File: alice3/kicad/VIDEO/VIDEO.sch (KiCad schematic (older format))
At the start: 14 parts, among them SW1 SW_PUSH, U1 Propeller_P8X32A-D40, U2 VGA_daughter_board, U3 24LC256, U4 Propeller_Plug, U5 LM2937-3.3, Y1 5 MHz

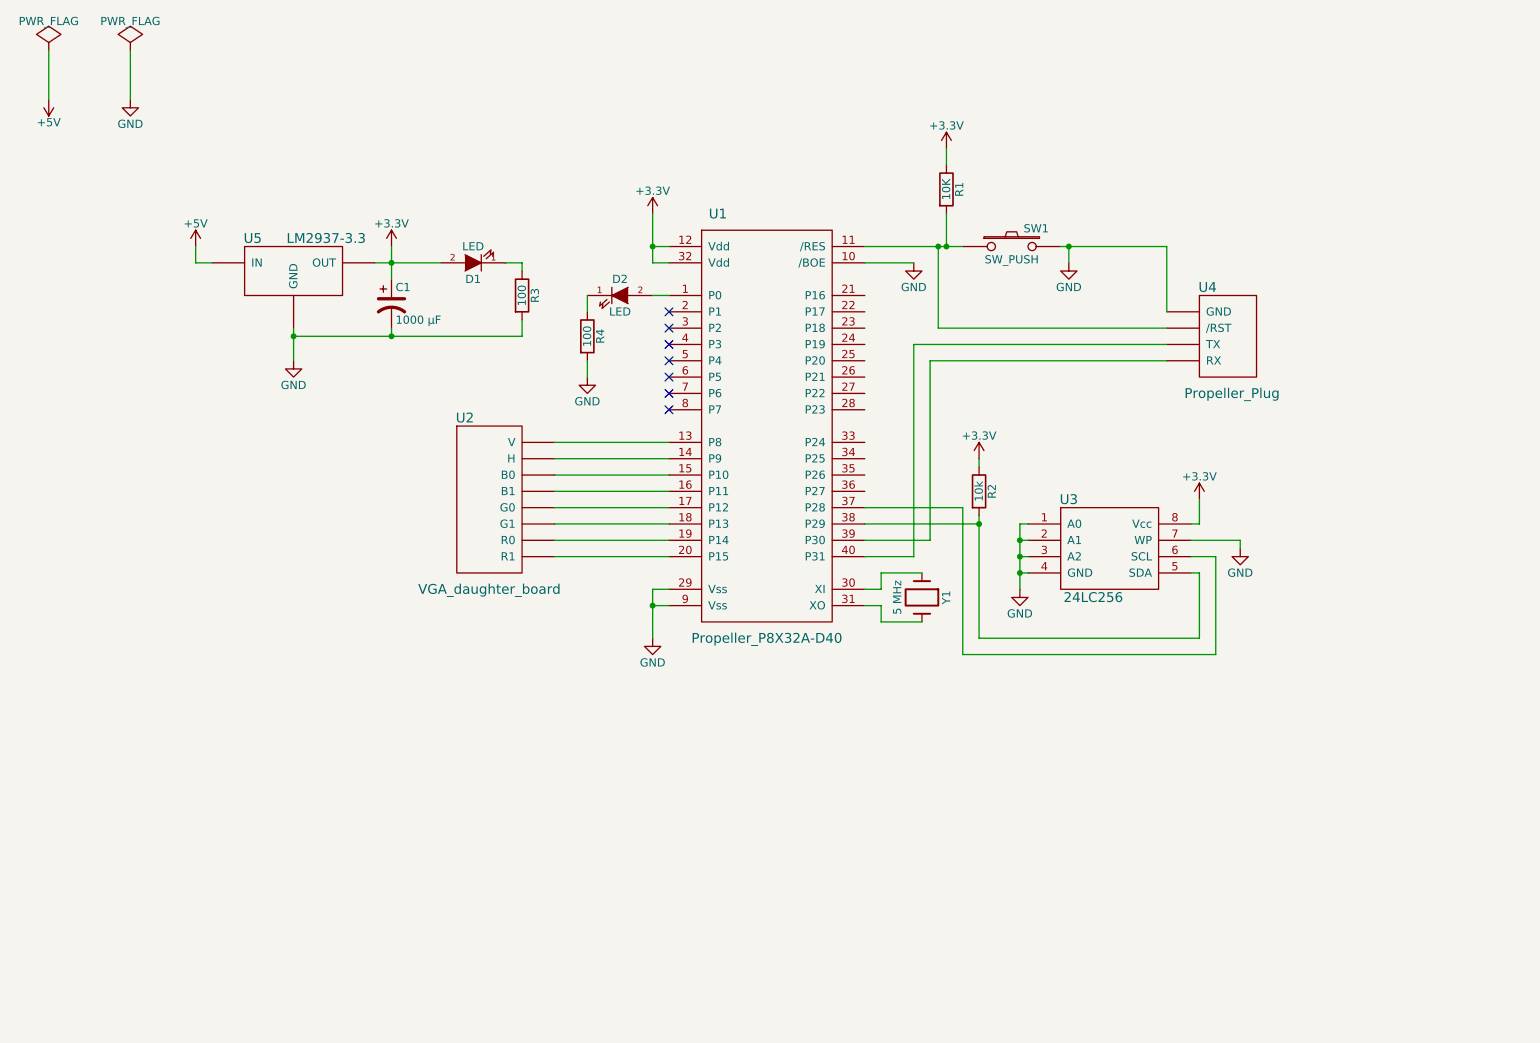
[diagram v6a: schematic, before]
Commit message: Add level shifters to video board.
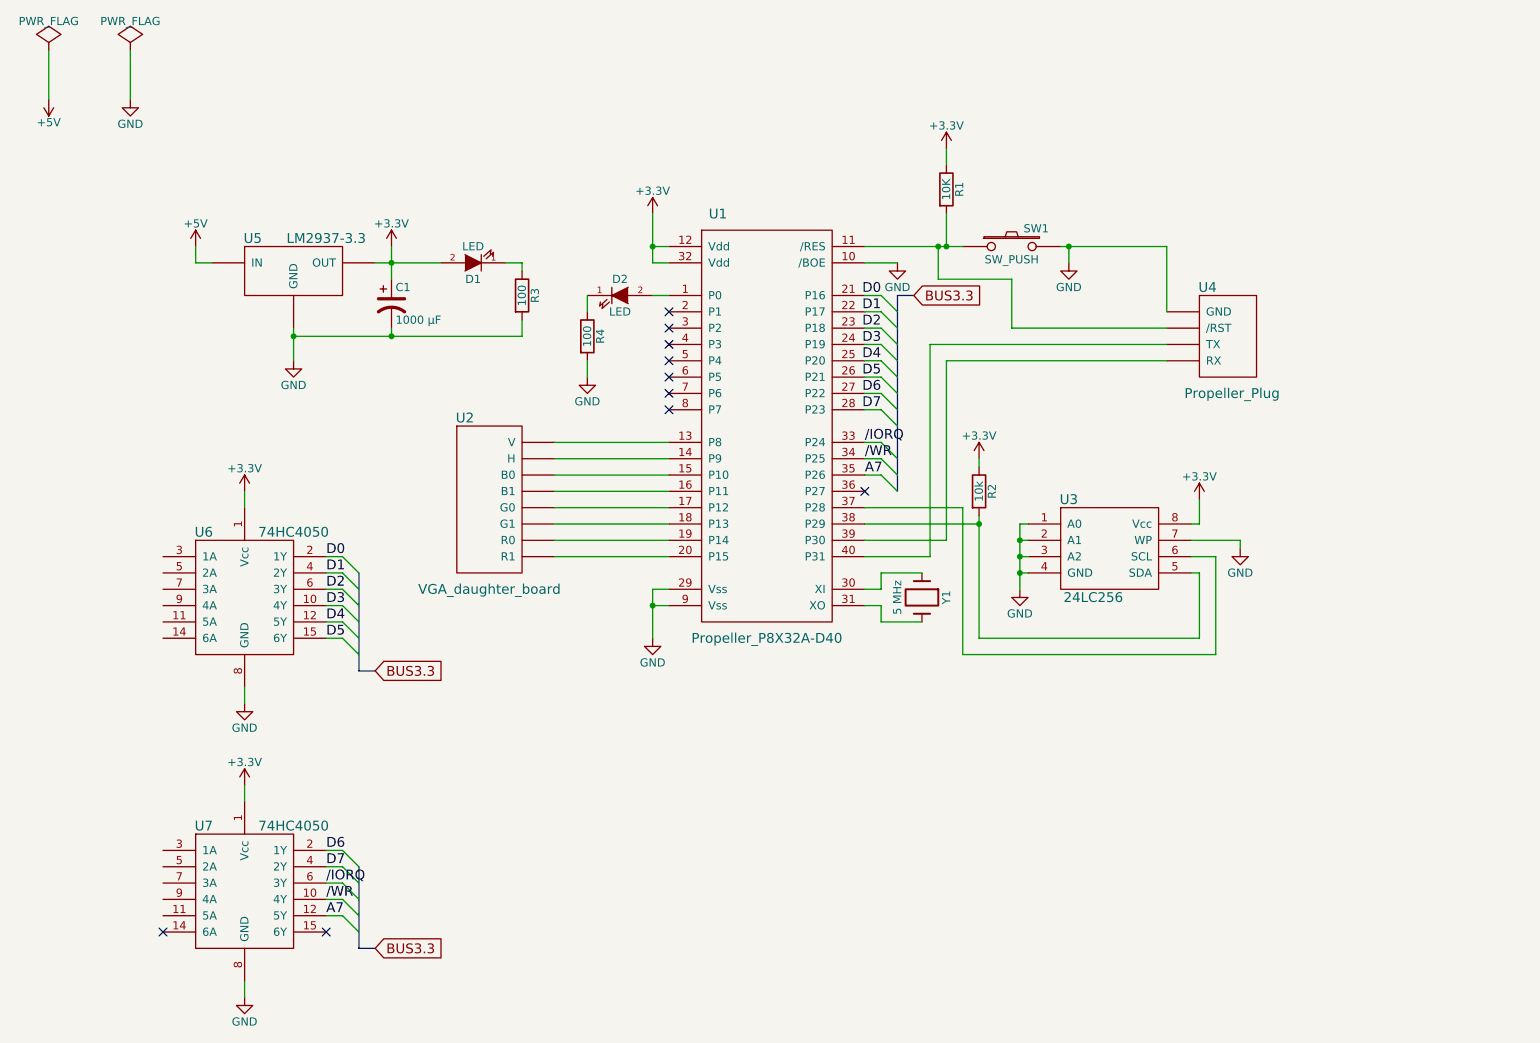
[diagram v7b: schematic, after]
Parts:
- added U6, U7: 74HC4050, symbol 74HC4050
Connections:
- net +3V3: now also U6.1 (Vcc), U7.1 (Vcc)
- net GND: now also U6.8 (GND), U7.8 (GND)
- net D0: now reaches U1.21 (P16)
- net D0: now also U6.2 (1Y)
- net D1: now reaches U1.22 (P17)
- net D1: now also U6.4 (2Y)
- net D2: now reaches U1.23 (P18)
- net D2: now also U6.6 (3Y)
- net D3: now reaches U1.24 (P19)
- net D3: now also U6.10 (4Y)
- net D4: now reaches U1.25 (P20)
- net D4: now also U6.12 (5Y)
- net D5: now reaches U1.26 (P21)
- net D5: now also U6.15 (6Y)
- net D6: now reaches U1.27 (P22)
- net D6: now also U7.2 (1Y)
- net D7: now reaches U1.28 (P23)
- net D7: now also U7.4 (2Y)
- net /IORQ: now reaches U1.33 (P24)
- net /IORQ: now also U7.6 (3Y)
- net /WR: now reaches U1.34 (P25)
- net /WR: now also U7.10 (4Y)
- net A7: now reaches U1.35 (P26)
- net A7: now also U7.12 (5Y)
- no-connect marks 7 -> 10

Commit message: Added bus.
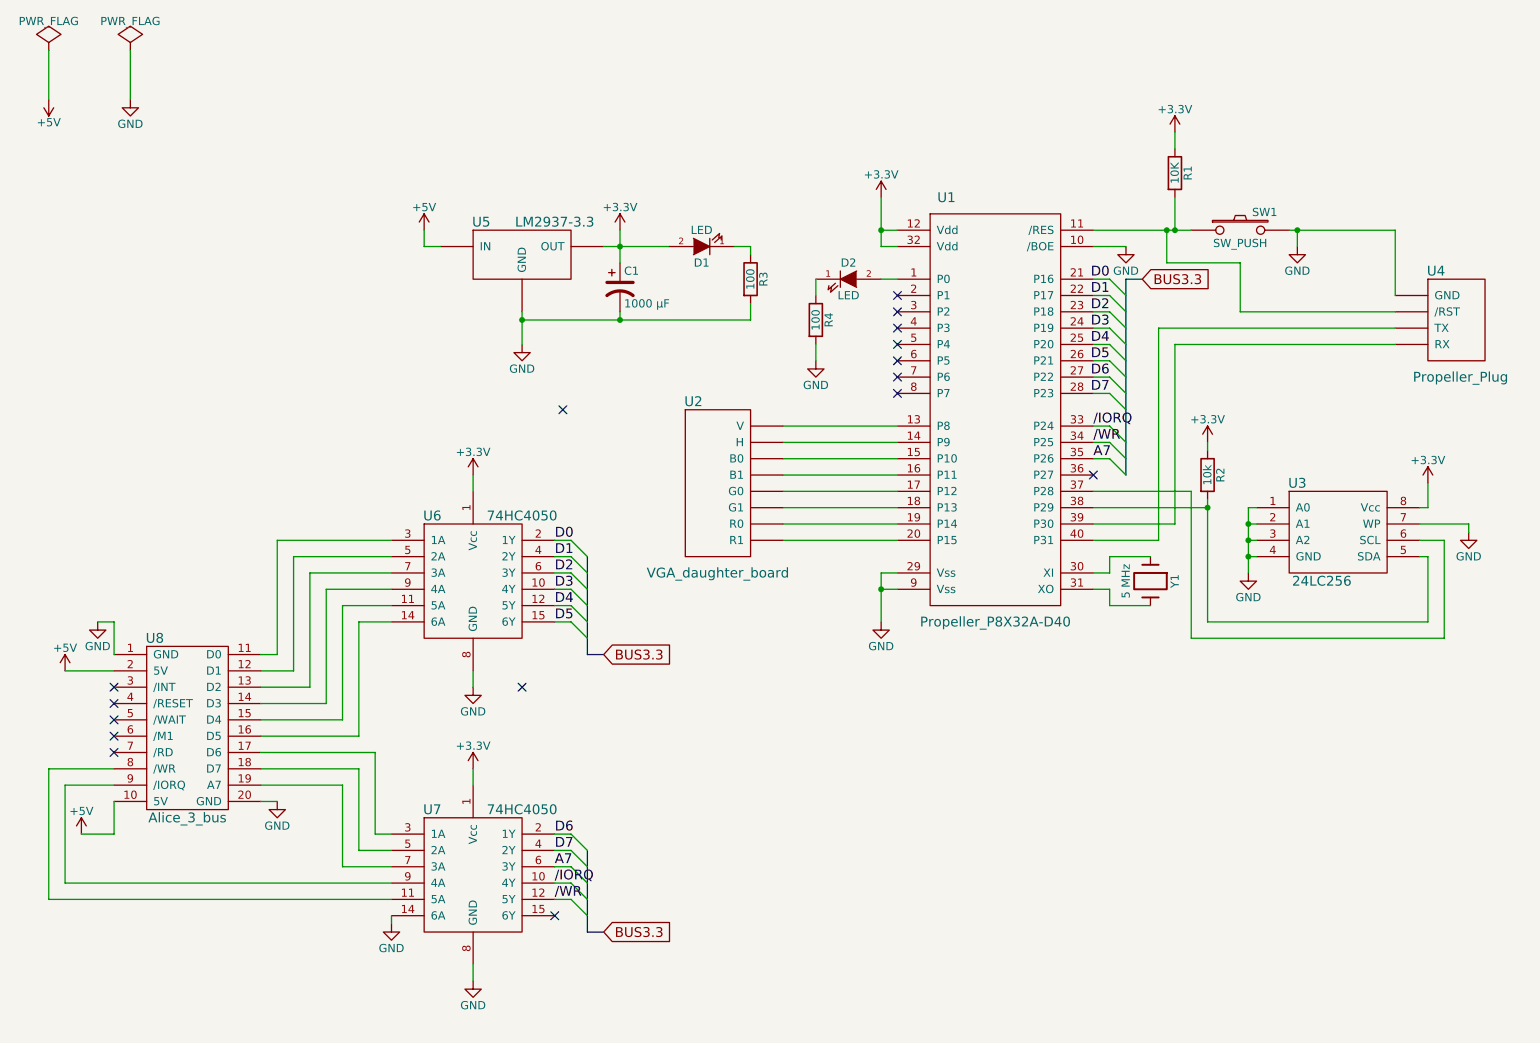
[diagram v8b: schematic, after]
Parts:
- added U8: Alice_3_bus, symbol Alice_3_bus-RESCUE-VIDEO
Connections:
- net +5V: now also U8.10 (5V), U8.2 (5V)
- net /IORQ: now also U7.10 (4Y); no longer U7.6 (3Y)
- net /WR: now also U7.12 (5Y); no longer U7.10 (4Y)
- net A7: now also U7.6 (3Y); no longer U7.12 (5Y)
- net GND: now also U7.14 (6A), U8.1 (GND), U8.20 (GND)
- net at U6.11 (5A): now also U8.15 (D4)
- net at U6.14 (6A): now also U8.16 (D5)
- net at U6.3 (1A): now also U8.11 (D0)
- net at U6.5 (2A): now also U8.12 (D1)
- net at U6.7 (3A): now also U8.13 (D2)
- net at U6.9 (4A): now also U8.14 (D3)
- net at U7.11 (5A): now also U8.8 (/WR)
- net at U7.3 (1A): now also U8.17 (D6)
- net at U7.5 (2A): now also U8.18 (D7)
- net at U7.7 (3A): now also U8.19 (A7)
- net at U7.9 (4A): now also U8.9 (/IORQ)
- no-connect marks 10 -> 16
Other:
- moved on the sheet: C1, D1, D2, R1, R2, R3, R4, SW1, U1, U2, U3, U4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
